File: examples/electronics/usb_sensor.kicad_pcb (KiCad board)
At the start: 40 x 30 mm, 17 parts, among them J1 USB-Micro-B, J2 SWD, SW1 SPST, U1 AP2112K-3.3, U2 STM32F042, U3 SHT40

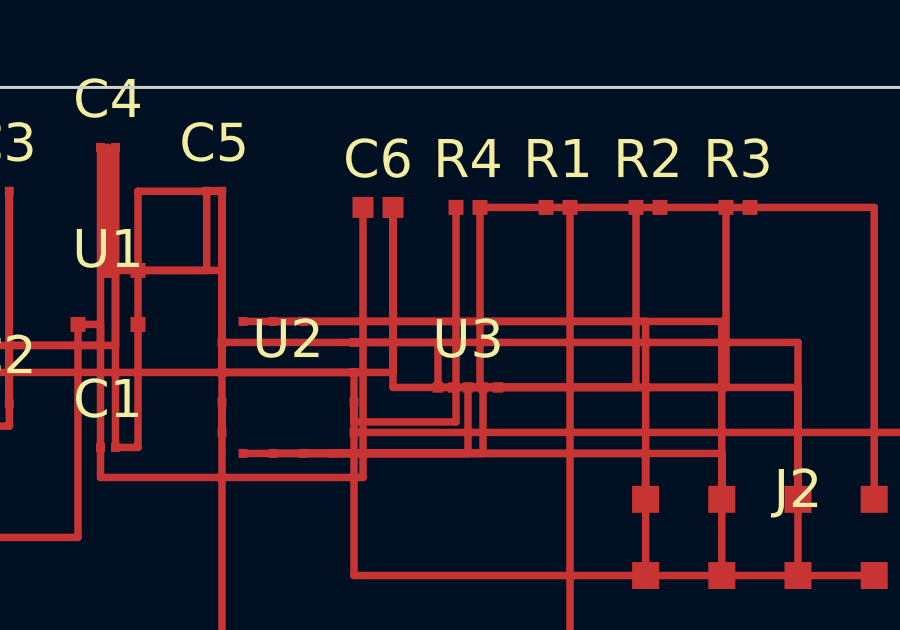
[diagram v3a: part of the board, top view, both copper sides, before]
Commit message: feat(electronics): SPST component modes and node state selection
Add explicitly named finite component modes to the law substrate:

- parse contextual `mode <name> { … }` declarations in component bodies
- elaborate mode facts through the shared linear-law machinery
- enumerate every declared mode as a first-class DC operating state
- record instance→mode assignments and deterministic state labels
- select node-applicable states with `sw1.closed` / `!sw1.closed`
- prove node postconditions only in matching states while tolerance,
  rating, and budget checks remain all-state
- reject unknown modes and mode preconditions matching zero states
- add generic stdlib Spst with closed/open modes
- migrate usb_sensor to Spst, split pressed/released nodes, wire the
  button pull-up path, and make its local resistor law-bearing

Checked-in .ebv fixtures cover pressed/released selection and a typoed
mode selector. Full lib suite green; electronics fixtures emit; no new
Praetor diagnostics in touched analysis/parser/backend surfaces.
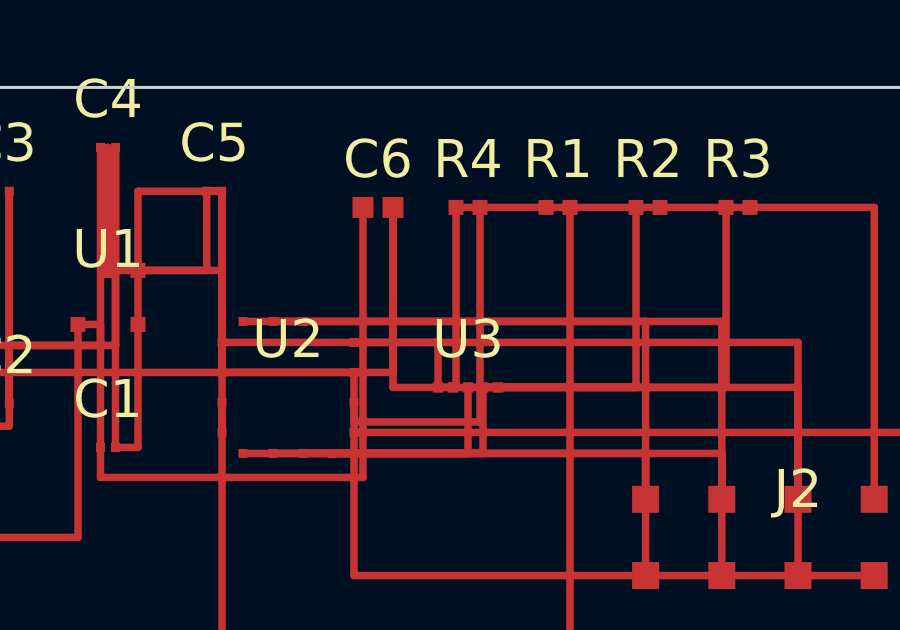
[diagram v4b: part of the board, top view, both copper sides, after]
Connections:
- R4 pad 1: N6 -> N5
- R4 pad 2: N5 -> N6
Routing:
- net V3.3: track 74.0 -> 171.7 mm
- net N6: track 29.5 -> 0.00 mm
- net N2: track 26.8 -> 0.00 mm
- net N4: track 22.3 -> 0.00 mm
- net N3: track 18.3 -> 0.00 mm
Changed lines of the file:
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@@
   (general (thickness 1.6))
   (net 1 "GND")
-  (net 2 "N2")
-  (net 3 "N3")
-  (net 4 "N4")
+  (net 2 "V3.3")
+  (net 3 "V3.3")
+  (net 4 "V3.3")
   (net 5 "V3.3")
-  (net 6 "N6")
+  (net 6 "V3.3")
   (net 7 "V5")
   (net 8 "N8")
@@
     (fp_text reference "R4" (at 0 -1.60) (layer "F.SilkS"))
     (fp_text value "10k" (at 0 1.60) (layer "F.Fab"))
-    (pad "1" smd rect (at -0.40 0.00) (size 0.50 0.50) (layers "F.Cu" "F.Paste" "F.Mask") (net 6 "N6"))
-    (pad "2" smd rect (at 0.40 0.00) (size 0.50 0.50) (layers "F.Cu" "F.Paste" "F.Mask") (net 5 "N5"))
+    (pad "1" smd rect (at -0.40 0.00) (size 0.50 0.50) (layers "F.Cu" "F.Paste" "F.Mask") (net 5 "N5"))
+    (pad "2" smd rect (at 0.40 0.00) (size 0.50 0.50) (layers "F.Cu" "F.Paste" "F.Mask") (net 6 "N6"))
   )
   (footprint "0603"
@@
   (segment (start 23.00 10.00) (end 33.00 10.00) (width 0.25) (layer "F.Cu") (net 1 "GND"))
   (segment (start 33.00 10.00) (end 33.00 13.73) (width 0.25) (layer "F.Cu") (net 1 "GND"))
-  (segment (start 19.60 25.00) (end 25.40 25.00) (width 0.25) (layer "F.Cu") (net 2 "N2"))
-  (segment (start 25.40 25.00) (end 25.40 4.00) (width 0.25) (layer "F.Cu") (net 2 "N2"))
-  (segment (start 17.50 12.20) (end 22.50 12.20) (width 0.25) (layer "F.Cu") (net 3 "N3"))
-  (segment (start 22.50 12.20) (end 22.50 10.00) (width 0.25) (layer "F.Cu") (net 3 "N3"))
-  (segment (start 22.50 10.00) (end 27.60 10.00) (width 0.25) (layer "F.Cu") (net 3 "N3"))
-  (segment (start 27.60 10.00) (end 27.60 4.00) (width 0.25) (layer "F.Cu") (net 3 "N3"))
-  (segment (start 16.50 12.20) (end 22.00 12.20) (width 0.25) (layer "F.Cu") (net 4 "N4"))
-  (segment (start 22.00 12.20) (end 22.00 10.00) (width 0.25) (layer "F.Cu") (net 4 "N4"))
-  (segment (start 22.00 10.00) (end 30.60 10.00) (width 0.25) (layer "F.Cu") (net 4 "N4"))
-  (segment (start 30.60 10.00) (end 30.60 4.00) (width 0.25) (layer "F.Cu") (net 4 "N4"))
+  (segment (start 19.60 25.00) (end 25.40 25.00) (width 0.25) (layer "F.Cu") (net 2 "V3.3"))
+  (segment (start 25.40 25.00) (end 25.40 4.00) (width 0.25) (layer "F.Cu") (net 2 "V3.3"))
+  (segment (start 17.50 12.20) (end 22.50 12.20) (width 0.25) (layer "F.Cu") (net 3 "V3.3"))
+  (segment (start 22.50 12.20) (end 22.50 10.00) (width 0.25) (layer "F.Cu") (net 3 "V3.3"))
+  (segment (start 22.50 10.00) (end 27.60 10.00) (width 0.25) (layer "F.Cu") (net 3 "V3.3"))
+  (segment (start 27.60 10.00) (end 27.60 4.00) (width 0.25) (layer "F.Cu") (net 3 "V3.3"))
+  (segment (start 16.50 12.20) (end 22.00 12.20) (width 0.25) (layer "F.Cu") (net 4 "V3.3"))
+  (segment (start 22.00 12.20) (end 22.00 10.00) (width 0.25) (layer "F.Cu") (net 4 "V3.3"))
+  (segment (start 22.00 10.00) (end 30.60 10.00) (width 0.25) (layer "F.Cu") (net 4 "V3.3"))
+  (segment (start 30.60 10.00) (end 30.60 4.00) (width 0.25) (layer "F.Cu") (net 4 "V3.3"))
   (segment (start 6.21 3.46) (end 6.21 3.46) (width 0.25) (layer "F.Cu") (net 5 "V3.3"))
   (segment (start 6.21 3.46) (end 6.21 10.54) (width 0.25) (layer "F.Cu") (net 5 "V3.3"))
@@
   (segment (start 13.80 8.50) (end 21.00 8.50) (width 0.25) (layer "F.Cu") (net 5 "V3.3"))
   (segment (start 21.00 8.50) (end 21.00 10.00) (width 0.25) (layer "F.Cu") (net 5 "V3.3"))
-  (segment (start 21.00 10.00) (end 22.40 10.00) (width 0.25) (layer "F.Cu") (net 5 "V3.3"))
-  (segment (start 22.40 10.00) (end 22.40 4.00) (width 0.25) (layer "F.Cu") (net 5 "V3.3"))
-  (segment (start 22.40 4.00) (end 24.60 4.00) (width 0.25) (layer "F.Cu") (net 5 "V3.3"))
+  (segment (start 21.00 10.00) (end 21.60 10.00) (width 0.25) (layer "F.Cu") (net 5 "V3.3"))
+  (segment (start 21.60 10.00) (end 21.60 4.00) (width 0.25) (layer "F.Cu") (net 5 "V3.3"))
+  (segment (start 21.60 4.00) (end 24.60 4.00) (width 0.25) (layer "F.Cu") (net 5 "V3.3"))
   (segment (start 24.60 4.00) (end 24.60 4.00) (width 0.25) (layer "F.Cu") (net 5 "V3.3"))
   (segment (start 24.60 4.00) (end 28.40 4.00) (width 0.25) (layer "F.Cu") (net 5 "V3.3"))
@@
   (segment (start 31.40 4.00) (end 35.54 4.00) (width 0.25) (layer "F.Cu") (net 5 "V3.3"))
   (segment (start 35.54 4.00) (end 35.54 13.73) (width 0.25) (layer "F.Cu") (net 5 "V3.3"))
-  (segment (start 3.40 7.00) (end 3.40 9.50) (width 0.25) (layer "F.Cu") (net 6 "N6"))
-  (segment (start 3.40 9.50) (end 18.20 9.50) (width 0.25) (layer "F.Cu") (net 6 "N6"))
-  (segment (start 18.20 9.50) (end 18.20 11.15) (width 0.25) (layer "F.Cu") (net 6 "N6"))
-  (segment (start 18.20 11.15) (end 21.60 11.15) (width 0.25) (layer "F.Cu") (net 6 "N6"))
-  (segment (start 21.60 11.15) (end 21.60 4.00) (width 0.25) (layer "F.Cu") (net 6 "N6"))
+  (segment (start 3.40 7.00) (end 3.40 9.50) (width 0.25) (layer "F.Cu") (net 6 "V3.3"))
+  (segment (start 3.40 9.50) (end 18.20 9.50) (width 0.25) (layer "F.Cu") (net 6 "V3.3"))
+  (segment (start 18.20 9.50) (end 18.20 11.15) (width 0.25) (layer "F.Cu") (net 6 "V3.3"))
+  (segment (start 18.20 11.15) (end 22.40 11.15) (width 0.25) (layer "F.Cu") (net 6 "V3.3"))
+  (segment (start 22.40 11.15) (end 22.40 4.00) (width 0.25) (layer "F.Cu") (net 6 "V3.3"))
   (segment (start 4.40 15.00) (end 9.00 15.00) (width 0.25) (layer "F.Cu") (net 7 "V5"))
   (segment (start 9.00 15.00) (end 9.00 7.90) (width 0.25) (layer "F.Cu") (net 7 "V5"))
